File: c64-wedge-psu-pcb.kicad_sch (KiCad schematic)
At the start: 23 parts, among them U1 LM2576T-ADJ

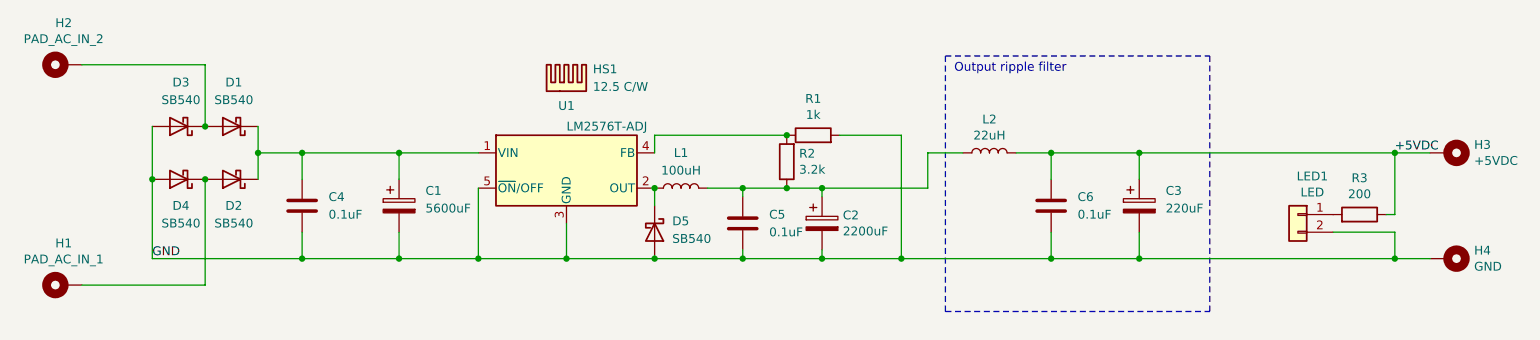
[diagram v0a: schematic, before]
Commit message: PCB rev 2.0: docs, KiCad, gerbers, and release caveat
README clarifies U1 placement against the wedge inner (middle) wall, documents bench results and BOM notes, and states that V2.0 will be tagged only after the latest board is built, verified, and re-measured. Measurement checklist HTML is updated to match.

KiCad schematic/PCB/BOM refresh, wedge silk graphic footprint, wedge.gif, regenerated gerbers, and new gerber archive (replaces 2026-03-29 export).
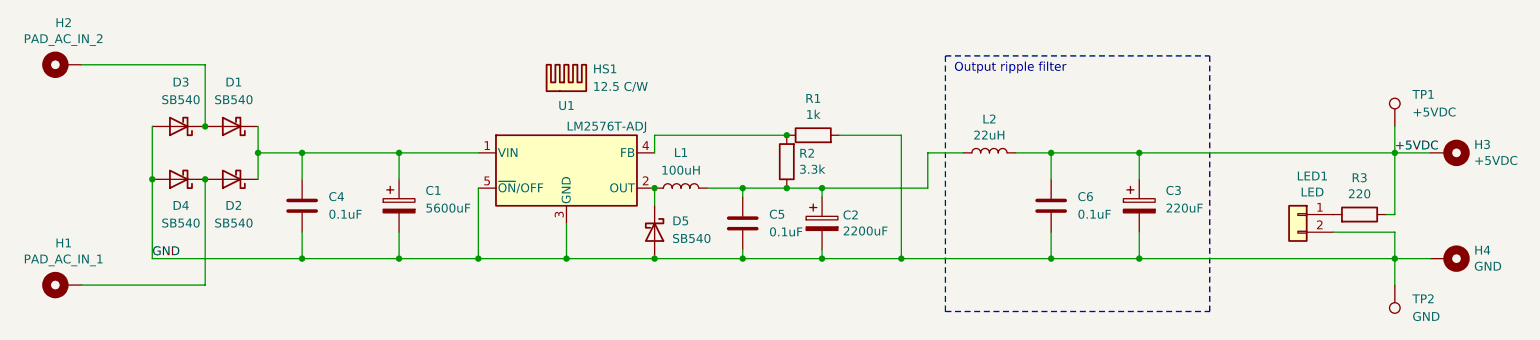
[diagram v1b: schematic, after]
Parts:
- added TP1: +5VDC, TestPoint:TestPoint_THTPad_2.0x2.0mm_Drill1.0mm, symbol Connector:TestPoint
- added TP2: GND, TestPoint:TestPoint_THTPad_2.0x2.0mm_Drill1.0mm, symbol Connector:TestPoint
- R2: value 3.2k -> 3.3k
- R3: value 200 -> 220
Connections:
- net +5VDC: now also TP1.1
- net GND: now also TP2.1
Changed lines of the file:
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@@
+	(wire
+		(pts
+			(xy 236.22 88.9) (xy 236.22 92.71)
+		)
+		(stroke
+			(width 0)
+			(type default)
+		)
+	)
 	(wire
 		(pts
@@
 		(pts
 			(xy 116.84 107.95) (xy 129.54 107.95)
+		)
+		(stroke
+			(width 0)
+			(type default)
+		)
+	)
+	(wire
+		(pts
+			(xy 236.22 107.95) (xy 236.22 111.76)
 		)
 		(stroke
@@
 			)
 		)
-		(property "Value" "200"
+		(property "Value" "220"
 			(at 231.14 98.6536 90)
 			(effects
@@
 			)
 		)
-		(property "Value" "3.2k"
+		(property "Value" "3.3k"
 			(at 150.368 95.123 0)
 			(effects
@@
 					(unit 1)
 				)
+			)
+		)
+	)
+	(symbol
+		(lib_id "Connector:TestPoint")
+		(at 236.22 111.76 180)
+		(unit 1)
+		(exclude_from_sim no)
+		(in_bom no)
+		(on_board yes)
+		(dnp no)
+		(fields_autoplaced yes)
+		(property "Reference" "TP2"
+			(at 238.76 113.7919 0)
+			(effects
+				(font
+					(size 1.27 1.27)
+				)
+				(justify right)
+			)
+		)
+		(property "Value" "GND"
+			(at 238.76 116.3319 0)
+			(effects
+				(font
+					(size 1.27 1.27)
+				)
+				(justify right)
+			)
+		)
+		(property "Footprint" "TestPoint:TestPoint_THTPad_2.0x2.0mm_Drill1.0mm"
+			(at 231.14 111.76 0)
+			(effects
+				(font
+					(size 1.27 1.27)
+				)
+				(hide yes)
+			)
+		)
+		(property "Datasheet" "~"
+			(at 231.14 111.76 0)
+			(effects
+				(font
+					(size 1.27 1.27)
+				)
+				(hide yes)
+			)
+		)
+		(property "Description" "test point"
+			(at 236.22 111.76 0)
+			(effects
+				(font
+					(size 1.27 1.27)
+				)
+				(hide yes)
+			)
+		)
+		(pin "1"
+		)
+		(instances
+			(project ""
+				(path "/25ef7e59-af8f-4cb3-8d4a-791b61806d46"
+					(reference "TP2")
+					(unit 1)
+				)
+			)
+		)
+	)
+	(symbol
+		(lib_id "Connector:TestPoint")
+		(at 236.22 88.9 0)
+		(unit 1)
+		(exclude_from_sim no)
+		(in_bom no)
+		(on_board yes)
+		(dnp no)
+		(fields_autoplaced yes)
+		(property "Reference" "TP1"
+			(at 238.76 84.3279 0)
+			(effects
+				(font
+					(size 1.27 1.27)
+				)
+				(justify left)
+			)
+		)
+		(property "Value" "+5VDC"
+			(at 238.76 86.8679 0)
+			(effects
+				(font
+					(size 1.27 1.27)
+				)
+				(justify left)
+			)
+		)
+		(property "Footprint" "TestPoint:TestPoint_THTPad_2.0x2.0mm_Drill1.0mm"
+			(at 241.3 88.9 0)
+			(effects
+				(font
+					(size 1.27 1.27)
+				)
+				(hide yes)
+			)
+		)
+		(property "Datasheet" "~"
+			(at 241.3 88.9 0)
+			(effects
+				(font
+					(size 1.27 1.27)
+				)
+				(hide yes)
+			)
+		)
+		(property "Description" "test point"
+			(at 236.22 88.9 0)
+			(effects
+				(font
+					(size 1.27 1.27)
+				)
+				(hide yes)
+			)
+		)
+		(pin "1"
+		)
+		(instances
+			(project ""
+				(path "/25ef7e59-af8f-4cb3-8d4a-791b61806d46"
+					(reference "TP1")
+					(unit 1)
+				)

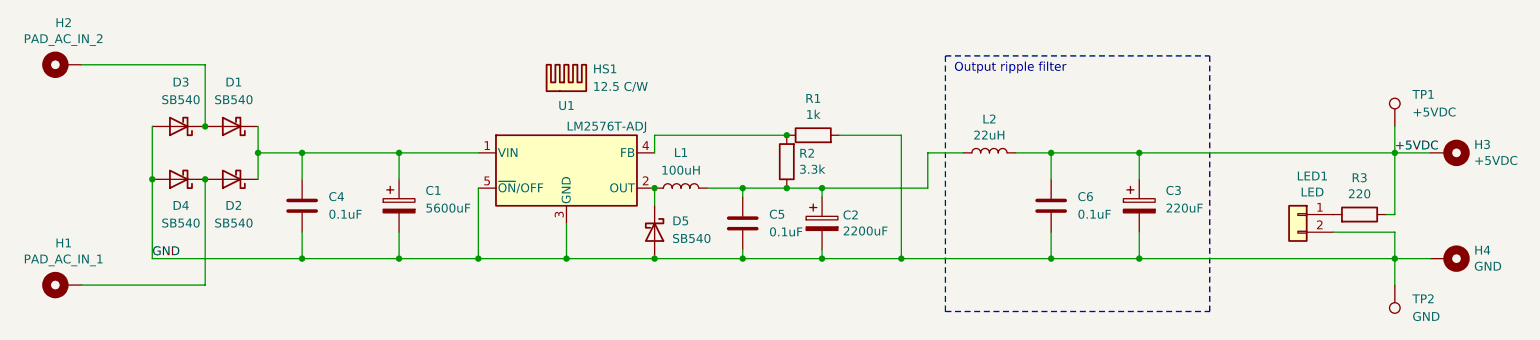
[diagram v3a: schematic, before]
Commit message: PCB update for added 3D case
added partial 3D model of the case (FreeCAD)
added heatsink footprint
added 3D model for some parts from the vendors
changed rectifier to single component
change board shape to fit snugly in the case
moved some stuff around to make it fit in the available space
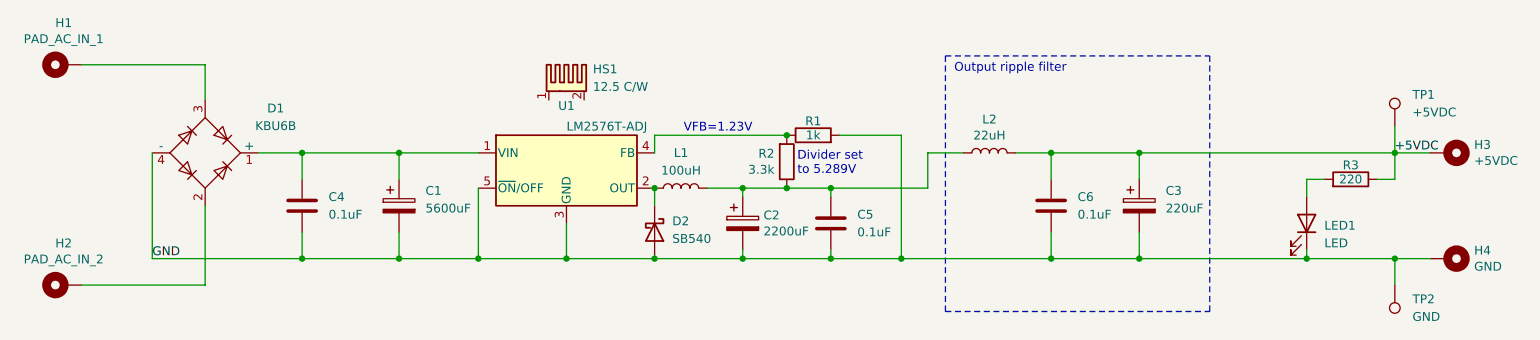
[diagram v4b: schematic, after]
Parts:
- removed D1, D2, D3, D4: SB540, Diode_THT:D_DO-201AD_P12.70mm_Horizontal, symbol Device:D_Schottky
- removed HS1: 12.5 C/W, symbol Mechanical:Heatsink
- removed LED1: LED, LED_THT:LED_D3.0mm, symbol Connector_Generic:Conn_01x02
- added D1: KBU6B, Diode_THT:Diode_Bridge_Vishay_KBU, symbol Diode_Bridge:KBU6B
- added HS1: 12.5 C/W, c64-wedge-psu-pcb:ATS-PCB1036, symbol Mechanical:Heatsink_Pad_2Pin
- added LED1: LED, LED_THT:LED_D3.0mm, symbol Device:LED
- C1: footprint Capacitor_THT:CP_Radial_D18.0mm_P7.50mm -> Capacitor_THT:CP_Radial_D16.0mm_P7.50mm
- renumbered D5 to D2
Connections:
- net GND: now also D1.4 (-), LED1.1 (K)
- net at C1.1, C4.1, U1.1 (VIN): now also D1.1 (+)
- net at R3.2: now also LED1.2 (A)
- net at H1.1: now also D1.3
- net at H2.1: now also D1.2
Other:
- note added: "Divider set to 5.289V"
- note added: "VFB=1.23V"
- moved on the sheet: C2, C5, H1, H2, R2, R3
